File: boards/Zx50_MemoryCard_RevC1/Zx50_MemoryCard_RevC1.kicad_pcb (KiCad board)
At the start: 6 copper layers, 132.1 x 107.9 mm, 247 parts, among them J1 2.5V, J10 RS232 5V, J11 RJ45_RB1-125B8G1A, J12 RJ45_RB1-125B8G1A, J2 3.3V, J3 Zx50_EdgeConnector, J4 TP_CLK, J5 TP_MCLK, J6 GND, J7 GND, J8 DEBUG, J9 JTAG 5V, Q1 2N7002, SW1 SW_DIP_x05, SW2 RESET, U1 AMS1117-2.5, U10 74LVC3G07, U11 74LVC245, U12 LCMXO3LF-6900C-5BG400C, U13 TXU0204PWR, U14 TXU0304PWR, U15 IS61WV10248EDBLL, U16 IS61WV10248EDBLL, U17 IS61WV10248EDBLL, U18 IS61WV10248EDBLL, U19 IS25LP080D-JNLE-TR, U2 AMS1117-3.3, U20 IS25LP080D-JNLE-TR, U21 74LVC245, U22 SN74LVC1G17DBVR, U23 74LVC245, U24 74LVC245, U3 74LVC245, U4 74LVC245, U5 74LVC245, U6 74LVC245, U7 74LVC1G17, U8 74LVC1G17, U9 74LVC245, Y1 25 MHz

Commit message: reorg firmware
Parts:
- added D14: RED, LED_SMD:LED_0805_2012Metric, F.Cu at (156.8, 121.9)
- added D15: BLUE, LED_SMD:LED_0805_2012Metric, F.Cu at (156.8, 124.5)
- added D16: BLUE, LED_SMD:LED_0805_2012Metric, F.Cu at (156.8, 127.0)
- added D17: BLUE, LED_SMD:LED_0805_2012Metric, F.Cu at (156.8, 129.5)
- added D18: BLUE, LED_SMD:LED_0805_2012Metric, F.Cu at (156.8, 132.1)
- added D19: GRN, LED_SMD:LED_0805_2012Metric, F.Cu at (156.8, 134.6)
- added D20: GRN, LED_SMD:LED_0805_2012Metric, F.Cu at (156.8, 137.2)
- R10, R11, R12, R13, R14, R8, R9: value 33 -> 330; footprint Resistor_SMD:R_0402_1005Metric -> Resistor_SMD:R_0805_2012Metric
- R41: value 33 -> 10k
- moved R14 114.3 mm to (152.4, 137.1), turned to 180 degrees
- moved R13 113.8 mm to (152.4, 134.6), turned to 180 degrees
- moved R12 113.4 mm to (152.4, 132.1), turned to 180 degrees
- moved R11 113.0 mm to (152.4, 129.5), turned to 180 degrees
- moved R10 112.5 mm to (152.4, 127.0), turned to 180 degrees
- moved R9 112.1 mm to (152.4, 124.5), turned to 180 degrees
- moved R8 111.6 mm to (152.4, 121.9), turned to 180 degrees
- moved D4 111.4 mm to (156.8, 114.3), turned to 180 degrees
- moved D5 111.1 mm to (156.8, 116.8), turned to 180 degrees
- moved R22 107.7 mm to (152.4, 111.8), turned to 180 degrees
- moved R21 102.6 mm to (152.4, 119.4), turned to 180 degrees
- moved R20 102.2 mm to (152.4, 116.8), turned to 180 degrees
- moved R19 101.8 mm to (152.4, 114.3), turned to 180 degrees
- moved D6 94.9 mm to (156.8, 119.4), turned to 180 degrees
- moved D3 94.8 mm to (156.8, 111.8), turned to 180 degrees
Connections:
- R10 pad 1: /D_DIR -> Net-(D16-A)
- R10 pad 2: unconnected-(R10-Pad2) -> +3.3V
- R11 pad 1: /~Z80_D_OE -> Net-(D17-A)
- R11 pad 2: unconnected-(R11-Pad2) -> +3.3V
- R12 pad 1: /FPGA/~WE -> Net-(D18-A)
- R12 pad 2: unconnected-(R12-Pad2) -> +3.3V
- R13 pad 1: /FPGA/~CE1 -> Net-(D19-A)
- R13 pad 2: unconnected-(R13-Pad2) -> +3.3V
- R14 pad 1: /FPGA/~CE0 -> Net-(D20-A)
- R14 pad 2: unconnected-(R14-Pad2) -> +3.3V
- R15 pad 1: /FPGA/~WE -> unconnected-(R15-Pad1)
- R16 pad 1: /FPGA/~CE0 -> unconnected-(R16-Pad1)
- R17 pad 1: /FPGA/~CE1 -> unconnected-(R17-Pad1)
- R18 pad 1: /FPGA/~CE2 -> unconnected-(R18-Pad1)
- R41 pad 1: unconnected-(R41-Pad1) -> /FPGA/CE3_LED_N
- R41 pad 2: /D_DIR -> +3.3V
- R8 pad 1: unconnected-(R8-Pad1) -> Net-(D14-A)
- R8 pad 2: /~SH_D_OE -> +3.3V
- R9 pad 1: unconnected-(R9-Pad1) -> Net-(D15-A)
- R9 pad 2: /FPGA/~OE -> +3.3V
- U12 pad L16: unconnected-(U12C-PR16C-PadL16) -> /FPGA/RAM2.A10
- U12 pad L17: unconnected-(U12C-PR12D-PadL17) -> /FPGA/RAM2.A19
- U12 pad L19: /FPGA/RAM1.A0 -> /FPGA/RAM2.A16
- U12 pad L20: unconnected-(U12D-PR15B-PadL20) -> /FPGA/RAM2.A15
- U12 pad M15: unconnected-(U12D-PR19C-PadM15) -> /FPGA/RAM2.A14
- U12 pad M16: unconnected-(U12D-PR17C-PadM16) -> /FPGA/RAM2.A13
- U12 pad M17: unconnected-(U12D-PR17A-PadM17) -> /FPGA/RAM2.A12
- U12 pad M18: unconnected-(U12D-PR16D-PadM18) -> /FPGA/RAM2.A11
- U12 pad M19: unconnected-(U12D-PR16B-PadM19) -> /FPGA/RAM2.A18
- U12 pad M20: unconnected-(U12D-PR16A-PadM20) -> /FPGA/RAM2.A17
- U12 pad N15: unconnected-(U12D-PR23C-PadN15) -> /FPGA/RAM2.A6
- U12 pad N16: unconnected-(U12D-PR21A-PadN16) -> /FPGA/RAM2.A7
- U12 pad N17: unconnected-(U12D-PR18B-PadN17) -> /FPGA/RAM2.A9
- U12 pad N18: unconnected-(U12D-PR18A-PadN18) -> /FPGA/RAM2.A8
- U12 pad N19: unconnected-(U12D-PR17D-PadN19) -> /FPGA/RAM2.D7
- U12 pad N20: unconnected-(U12D-PR17B-PadN20) -> /FPGA/RAM2.OE_N
- U12 pad P15: unconnected-(U12D-PR24C-PadP15) -> /FPGA/RAM2.A2
- U12 pad P16: unconnected-(U12D-PR23B-PadP16) -> /FPGA/RAM2.A3
- U12 pad P17: unconnected-(U12D-PR22B-PadP17) -> /FPGA/RAM2.A5
- U12 pad P18: unconnected-(U12D-PR19A-PadP18) -> /FPGA/RAM2.A4
- U12 pad P19: unconnected-(U12D-PR18D-PadP19) -> /FPGA/RAM2.D5
- U12 pad P20: unconnected-(U12D-PR18C-PadP20) -> /FPGA/RAM2.D6
- U12 pad R16: unconnected-(U12D-PR24D-PadR16) -> /FPGA/RAM2.A0
- U12 pad R17: unconnected-(U12D-PR24A-PadR17) -> /FPGA/RAM2.A1
- U12 pad R19: unconnected-(U12D-PR21B-PadR19) -> /FPGA/RAM2.WE_N
- U12 pad R20: unconnected-(U12D-PR19B-PadR20) -> /FPGA/RAM2.D4
- U12 pad T19: unconnected-(U12D-PR21D-PadT19) -> /FPGA/RAM2.D2
- U12 pad T20: unconnected-(U12D-PR21C-PadT20) -> /FPGA/RAM2.D3
- U12 pad U19: unconnected-(U12D-PR22D-PadU19) -> /FPGA/RAM2.D0
- U12 pad U20: unconnected-(U12D-PR22A-PadU20) -> /FPGA/RAM2.D1
- U12 pad V20: unconnected-(U12D-PR23A-PadV20) -> /FPGA/RAM2.CE_N
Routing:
- net /FPGA/RAM2.A9: track 0.00 -> 32.3 mm, vias 0 -> 2
- net /FPGA/RAM2.A7: track 0.00 -> 31.7 mm, vias 0 -> 2
- net /FPGA/RAM2.A6: track 0.00 -> 31.7 mm, vias 0 -> 2
- net /FPGA/RAM1.A19: track 32.2 -> 0.57 mm, vias 2 -> 1
- net /FPGA/RAM2.A8: track 0.00 -> 30.4 mm, vias 0 -> 2
- net /FPGA/RAM1.A10: track 30.7 -> 0.57 mm, vias 2 -> 1
- net /FPGA/RAM1.A11: track 30.2 -> 0.57 mm, vias 2 -> 1
- net /FPGA/RAM2.A10: track 0.00 -> 29.5 mm, vias 0 -> 2
- net /FPGA/RAM2.A19: track 0.00 -> 29.5 mm, vias 0 -> 2
- net /FPGA/RAM1.A12: track 30.0 -> 0.57 mm, vias 2 -> 1
- net /FPGA/RAM2.A5: track 0.00 -> 29.0 mm, vias 0 -> 2
- net /FPGA/RAM1.A9: track 28.5 -> 0.57 mm, vias 2 -> 1
- net /FPGA/RAM1.A8: track 28.2 -> 0.57 mm, vias 2 -> 1
- net /FPGA/RAM2.A11: track 0.00 -> 26.3 mm, vias 0 -> 2
- net /FPGA/RAM2.A13: track 0.00 -> 26.1 mm, vias 0 -> 2
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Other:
- board text added: "DBG1"
- board text added: "DBG2"
- board text added: "DBG3"
- board text added: "RAM0"
- board text added: "RAM1"
- board text added: "RAM2"
- board text added: "RAM3"
- board text added: "ROM0"
- board text added: "ROM1"
- board text added: "WE"

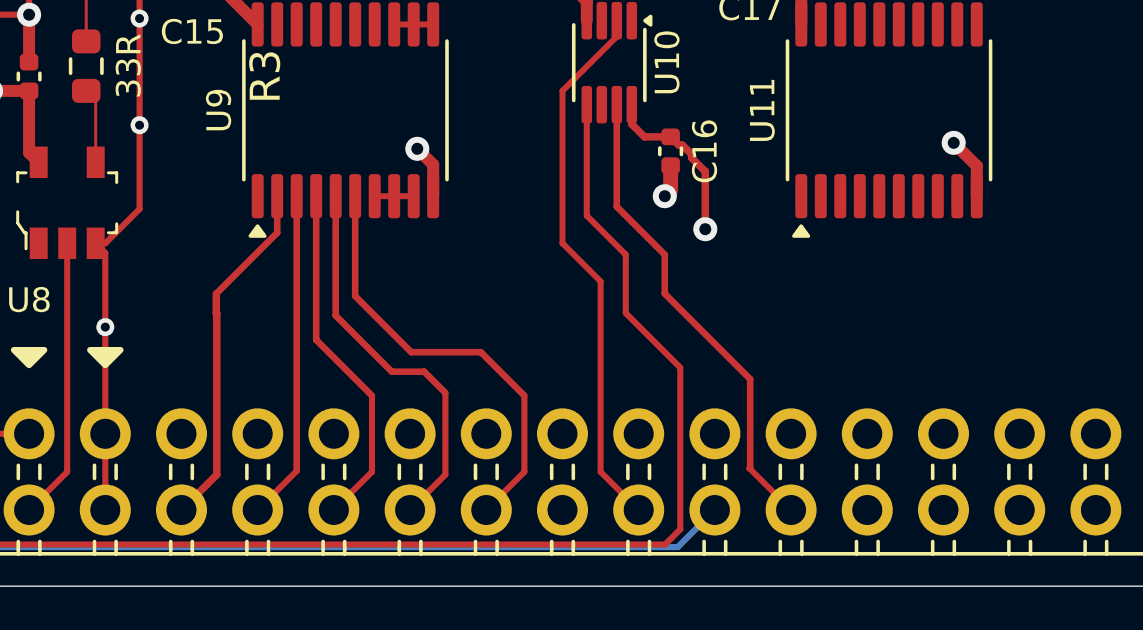
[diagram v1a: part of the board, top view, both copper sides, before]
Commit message: fireware fixes for serial card and getting pico-pic async working better.
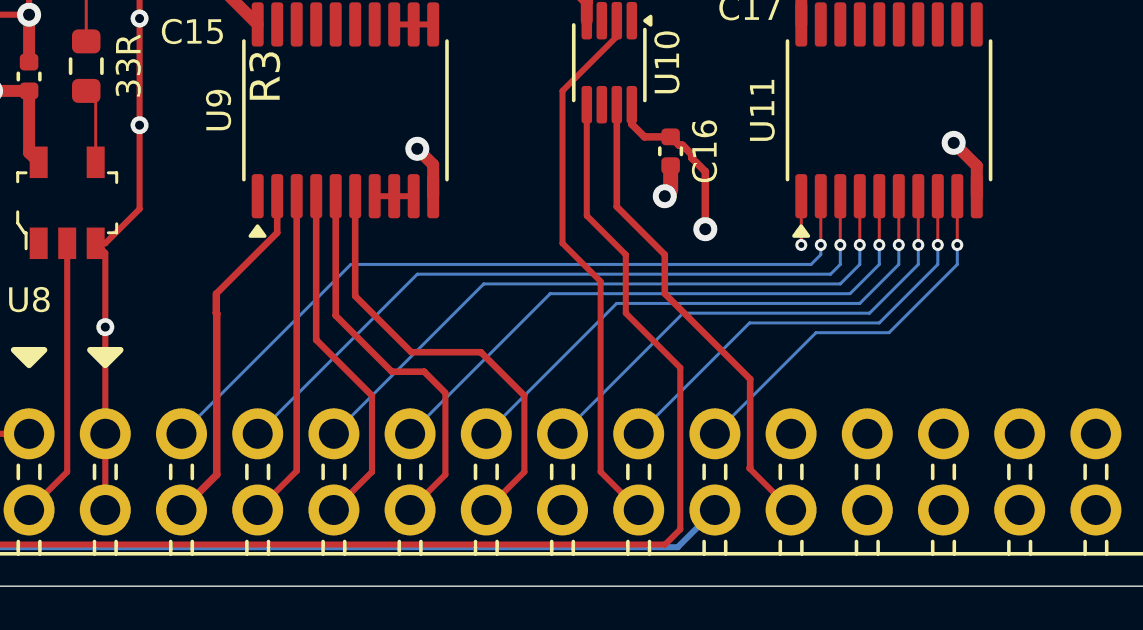
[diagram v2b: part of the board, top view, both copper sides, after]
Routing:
- net /SD0: track 0.00 -> 25.7 mm, vias 0 -> 1
- net /SD1: track 0.00 -> 24.0 mm, vias 0 -> 1
- net /SD2: track 0.00 -> 22.1 mm, vias 0 -> 1
- net /SD3: track 0.00 -> 20.3 mm, vias 0 -> 1
- net /SD4: track 0.00 -> 18.4 mm, vias 0 -> 1
- net /SD5: track 0.00 -> 16.5 mm, vias 0 -> 1
- net /SD6: track 0.00 -> 14.6 mm, vias 0 -> 1
- net /SD7: track 0.00 -> 12.7 mm, vias 0 -> 1
- net /D_DIR: track 43.7 -> 45.4 mm, vias 0 -> 1
